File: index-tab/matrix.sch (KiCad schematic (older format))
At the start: 0 parts

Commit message: Added MX alps hybrid symbol to the library
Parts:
- added MX? (x76): MX-LED, symbol MX_Alps_Hybrid:MX-LED

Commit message: Trying to make the library path indepented
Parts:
- MX? (x76): symbol MX_Alps_Hybrid:MX-LED -> index-tab-rescue:MX-LED-MX_Alps_Hybrid

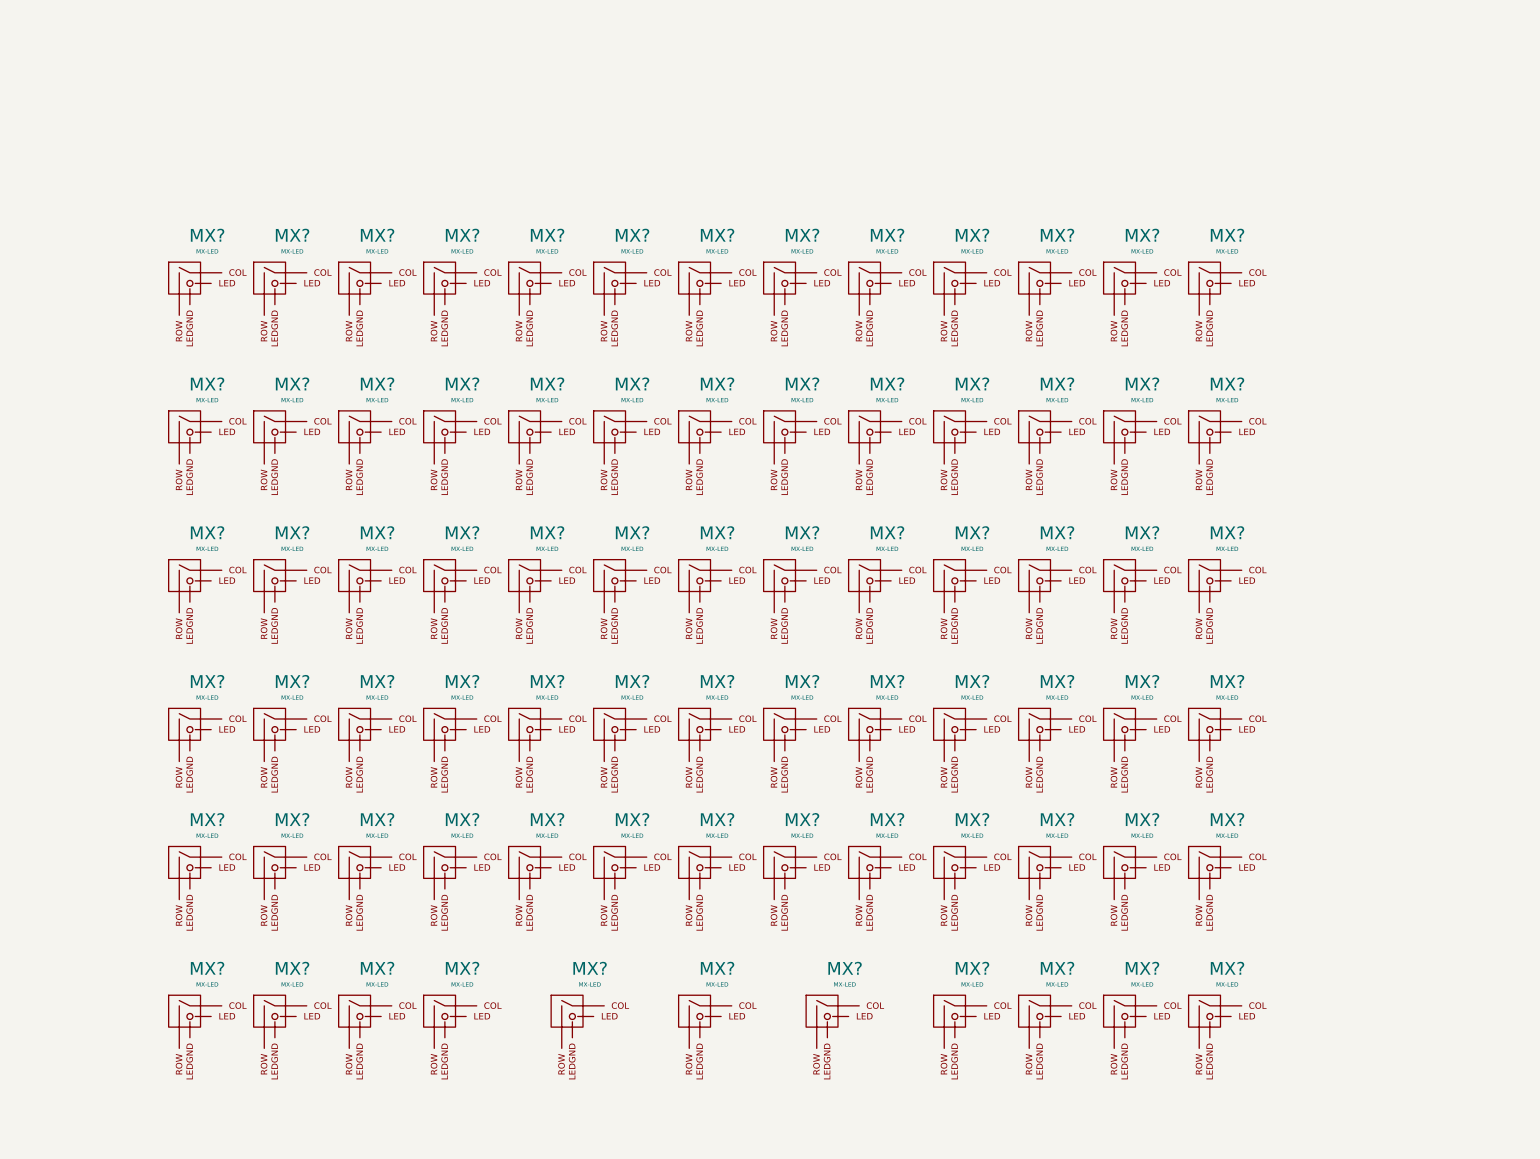
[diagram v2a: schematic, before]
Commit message: Change to u4, added files for backlight and rgb
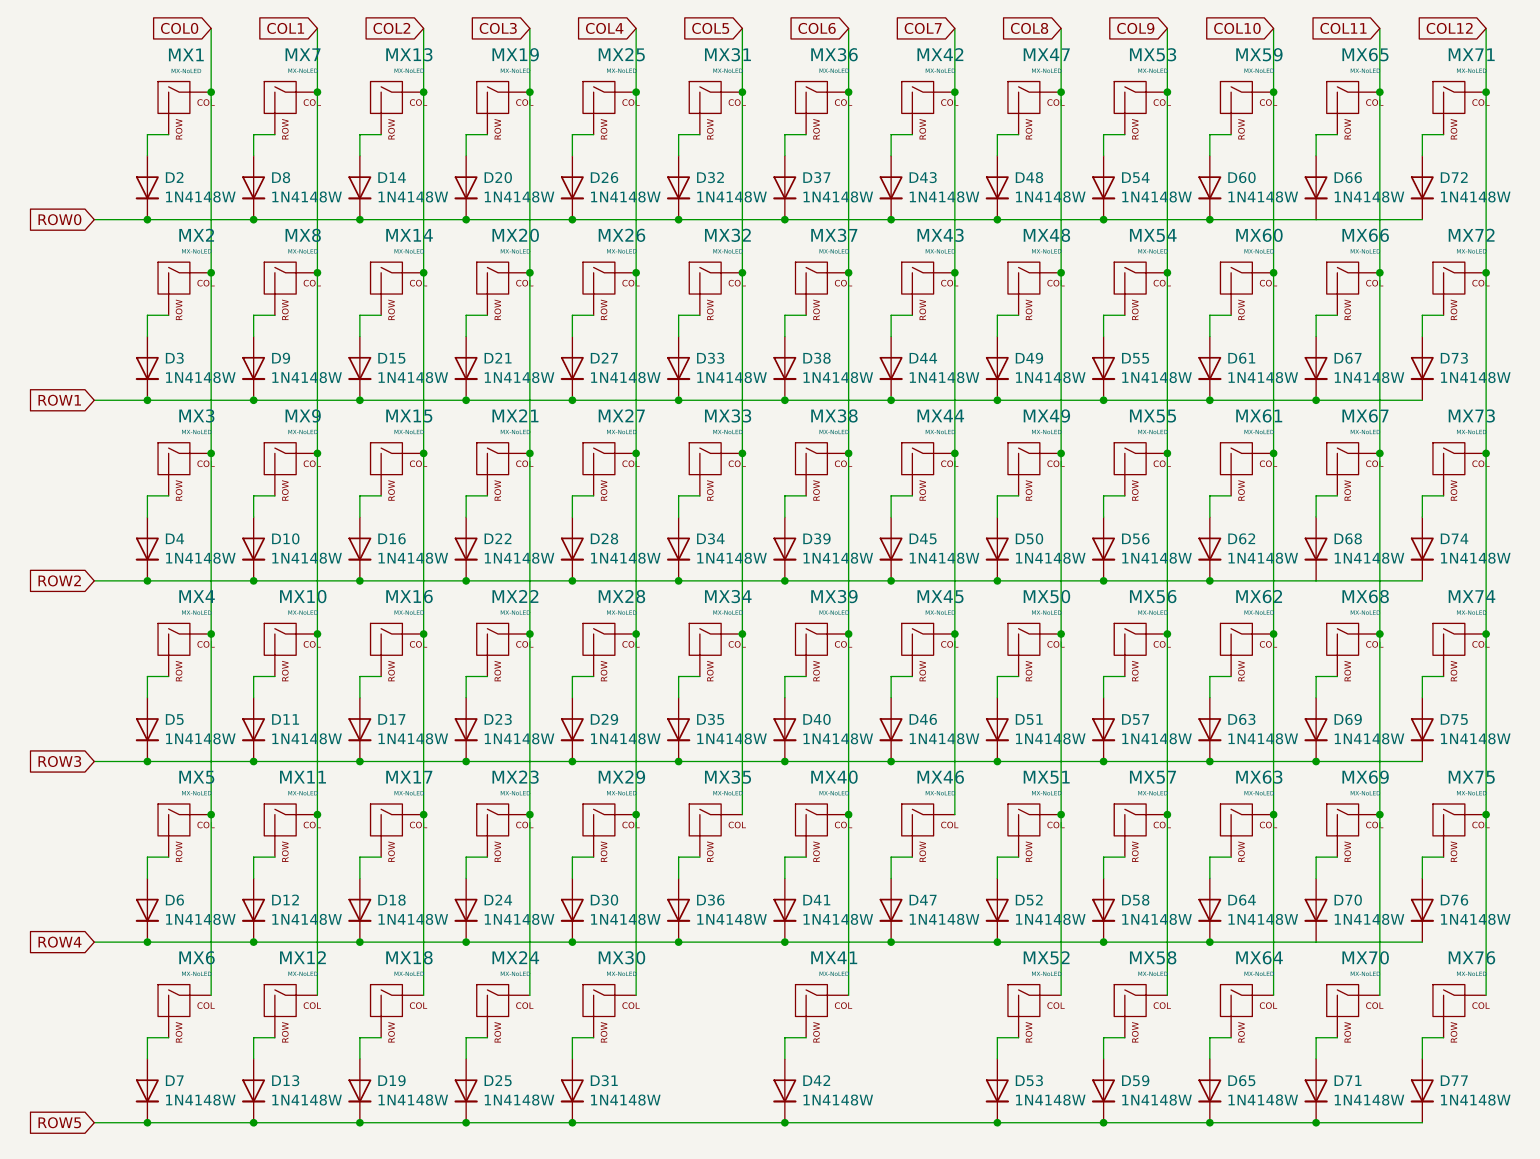
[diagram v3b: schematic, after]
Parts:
- removed MX? (x76): MX-LED, symbol index-tab-rescue:MX-LED-MX_Alps_Hybrid
- added D10, D11, D12, D13, D14, D15, D16, D17, D18, D19, D2, D20, D21, D22, D23, D24, D25, D26, D27, D28, D29, D3, D30, D31, D32, D33, D34, D35, D36, D37, D38, D39, D4, D40, D41, D42, D43, D44, D45, D46, D47, D48, D49, D5, D50, D51, D52, D53, D54, D55, D56, D57, D58, D59, D6, D60, D61, D62, D63, D64, D65, D66, D67, D68, D69, D7, D70, D71, D72, D73, D74, D75, D76, D77, D8, D9: 1N4148W, Diode_SMD:D_SOD-123, symbol Diode:1N4148W
- added MX1, MX10, MX11, MX12, MX13, MX14, MX15, MX16, MX17, MX18, MX19, MX2, MX20, MX21, MX22, MX23, MX24, MX25, MX26, MX27, MX28, MX29, MX3, MX30, MX31, MX32, MX33, MX34, MX35, MX36, MX37, MX38, MX39, MX4, MX40, MX41, MX42, MX43, MX44, MX45, MX46, MX47, MX48, MX49, MX5, MX50, MX51, MX52, MX53, MX54, MX55, MX56, MX57, MX58, MX59, MX6, MX60, MX61, MX62, MX63, MX64, MX65, MX66, MX67, MX68, MX69, MX7, MX70, MX71, MX72, MX73, MX74, MX75, MX76, MX8, MX9: MX-NoLED, symbol MX_Alps_Hybrid:MX-NoLED
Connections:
- new net: D2.2 (A), MX1.2 (ROW)
- new net: D8.2 (A), MX7.2 (ROW)
- new net: D14.2 (A), MX13.2 (ROW)
- new net: D20.2 (A), MX19.2 (ROW)
- new net: D26.2 (A), MX25.2 (ROW)
- new net: D32.2 (A), MX31.2 (ROW)
- new net: D37.2 (A), MX36.2 (ROW)
- new net: D43.2 (A), MX42.2 (ROW)
- new net: D48.2 (A), MX47.2 (ROW)
- new net: D54.2 (A), MX53.2 (ROW)
- new net: D60.2 (A), MX59.2 (ROW)
- new net: D66.2 (A), MX65.2 (ROW)
- new net: D72.2 (A), MX71.2 (ROW)
- new net: D3.2 (A), MX2.2 (ROW)
- new net: D9.2 (A), MX8.2 (ROW)
- new net: D15.2 (A), MX14.2 (ROW)
- new net: D21.2 (A), MX20.2 (ROW)
- new net: D27.2 (A), MX26.2 (ROW)
- new net: D33.2 (A), MX32.2 (ROW)
- new net: D38.2 (A), MX37.2 (ROW)
- new net: D44.2 (A), MX43.2 (ROW)
- new net: D49.2 (A), MX48.2 (ROW)
- new net: D55.2 (A), MX54.2 (ROW)
- new net: D61.2 (A), MX60.2 (ROW)
- new net: D67.2 (A), MX66.2 (ROW)
- new net: D73.2 (A), MX72.2 (ROW)
- new net: D4.2 (A), MX3.2 (ROW)
- new net: D10.2 (A), MX9.2 (ROW)
- new net: D16.2 (A), MX15.2 (ROW)
- new net: D22.2 (A), MX21.2 (ROW)
- new net: D28.2 (A), MX27.2 (ROW)
- new net: D34.2 (A), MX33.2 (ROW)
- new net: D39.2 (A), MX38.2 (ROW)
- new net: D45.2 (A), MX44.2 (ROW)
- new net: D50.2 (A), MX49.2 (ROW)
- new net: D56.2 (A), MX55.2 (ROW)
- new net: D62.2 (A), MX61.2 (ROW)
- new net: D68.2 (A), MX67.2 (ROW)
- new net: D74.2 (A), MX73.2 (ROW)
- new net: D5.2 (A), MX4.2 (ROW)
- new net: D11.2 (A), MX10.2 (ROW)
- new net: D17.2 (A), MX16.2 (ROW)
- new net: D23.2 (A), MX22.2 (ROW)
- new net: D29.2 (A), MX28.2 (ROW)
- new net: D35.2 (A), MX34.2 (ROW)
- new net: D40.2 (A), MX39.2 (ROW)
- new net: D46.2 (A), MX45.2 (ROW)
- new net: D51.2 (A), MX50.2 (ROW)
- new net: D57.2 (A), MX56.2 (ROW)
- new net: D63.2 (A), MX62.2 (ROW)
- new net: D69.2 (A), MX68.2 (ROW)
- new net: D75.2 (A), MX74.2 (ROW)
- new net: D6.2 (A), MX5.2 (ROW)
- new net: D12.2 (A), MX11.2 (ROW)
- new net: D18.2 (A), MX17.2 (ROW)
- new net: D24.2 (A), MX23.2 (ROW)
- new net: D30.2 (A), MX29.2 (ROW)
- new net: D36.2 (A), MX35.2 (ROW)
- new net: D41.2 (A), MX40.2 (ROW)
- new net: D47.2 (A), MX46.2 (ROW)
- new net: D52.2 (A), MX51.2 (ROW)
- new net: D58.2 (A), MX57.2 (ROW)
- new net: D64.2 (A), MX63.2 (ROW)
- new net: D70.2 (A), MX69.2 (ROW)
- new net: D76.2 (A), MX75.2 (ROW)
- new net: D7.2 (A), MX6.2 (ROW)
- new net: D13.2 (A), MX12.2 (ROW)
- new net: D19.2 (A), MX18.2 (ROW)
- new net: D25.2 (A), MX24.2 (ROW)
- new net: D31.2 (A), MX30.2 (ROW)
- new net: D42.2 (A), MX41.2 (ROW)
- new net: D53.2 (A), MX52.2 (ROW)
- new net: D59.2 (A), MX58.2 (ROW)
- new net: D65.2 (A), MX64.2 (ROW)
- new net: D71.2 (A), MX70.2 (ROW)
- new net: D77.2 (A), MX76.2 (ROW)
- new net COL0: MX1.1 (COL), MX2.1 (COL), MX3.1 (COL), MX4.1 (COL), MX5.1 (COL), MX6.1 (COL)
- new net COL1: MX10.1 (COL), MX11.1 (COL), MX12.1 (COL), MX7.1 (COL), MX8.1 (COL), MX9.1 (COL)
- new net COL10: MX59.1 (COL), MX60.1 (COL), MX61.1 (COL), MX62.1 (COL), MX63.1 (COL), MX64.1 (COL)
- new net COL11: MX65.1 (COL), MX66.1 (COL), MX67.1 (COL), MX68.1 (COL), MX69.1 (COL), MX70.1 (COL)
- new net COL12: MX71.1 (COL), MX72.1 (COL), MX73.1 (COL), MX74.1 (COL), MX75.1 (COL), MX76.1 (COL)
- new net COL2: MX13.1 (COL), MX14.1 (COL), MX15.1 (COL), MX16.1 (COL), MX17.1 (COL), MX18.1 (COL)
- new net COL3: MX19.1 (COL), MX20.1 (COL), MX21.1 (COL), MX22.1 (COL), MX23.1 (COL), MX24.1 (COL)
- new net COL4: MX25.1 (COL), MX26.1 (COL), MX27.1 (COL), MX28.1 (COL), MX29.1 (COL), MX30.1 (COL)
- new net COL5: MX31.1 (COL), MX32.1 (COL), MX33.1 (COL), MX34.1 (COL), MX35.1 (COL)
- new net COL6: MX36.1 (COL), MX37.1 (COL), MX38.1 (COL), MX39.1 (COL), MX40.1 (COL), MX41.1 (COL)
- new net COL7: MX42.1 (COL), MX43.1 (COL), MX44.1 (COL), MX45.1 (COL), MX46.1 (COL)
- new net COL8: MX47.1 (COL), MX48.1 (COL), MX49.1 (COL), MX50.1 (COL), MX51.1 (COL), MX52.1 (COL)
- new net COL9: MX53.1 (COL), MX54.1 (COL), MX55.1 (COL), MX56.1 (COL), MX57.1 (COL), MX58.1 (COL)
- new net ROW0: D14.1 (K), D2.1 (K), D20.1 (K), D26.1 (K), D32.1 (K), D37.1 (K), D43.1 (K), D48.1 (K), D54.1 (K), D60.1 (K), D66.1 (K), D72.1 (K), D8.1 (K)
- new net ROW1: D15.1 (K), D21.1 (K), D27.1 (K), D3.1 (K), D33.1 (K), D38.1 (K), D44.1 (K), D49.1 (K), D55.1 (K), D61.1 (K), D67.1 (K), D73.1 (K), D9.1 (K)
- new net ROW2: D10.1 (K), D16.1 (K), D22.1 (K), D28.1 (K), D34.1 (K), D39.1 (K), D4.1 (K), D45.1 (K), D50.1 (K), D56.1 (K), D62.1 (K), D68.1 (K), D74.1 (K)
- new net ROW3: D11.1 (K), D17.1 (K), D23.1 (K), D29.1 (K), D35.1 (K), D40.1 (K), D46.1 (K), D5.1 (K), D51.1 (K), D57.1 (K), D63.1 (K), D69.1 (K), D75.1 (K)
- new net ROW4: D12.1 (K), D18.1 (K), D24.1 (K), D30.1 (K), D36.1 (K), D41.1 (K), D47.1 (K), D52.1 (K), D58.1 (K), D6.1 (K), D64.1 (K), D70.1 (K), D76.1 (K)
- new net ROW5: D13.1 (K), D19.1 (K), D25.1 (K), D31.1 (K), D42.1 (K), D53.1 (K), D59.1 (K), D65.1 (K), D7.1 (K), D71.1 (K), D77.1 (K)

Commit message: Added footprints to all components, and done some formatting
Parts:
- MX1, MX10, MX11, MX12, MX13, MX14, MX15, MX16, MX17, MX18, MX19, MX2, MX20, MX21, MX22, MX23, MX24, MX25, MX26, MX27, MX28, MX29, MX3, MX31, MX32, MX33, MX34, MX35, MX36, MX37, MX38, MX39, MX4, MX40, MX41, MX42, MX43, MX44, MX45, MX46, MX47, MX48, MX49, MX5, MX50, MX51, MX53, MX54, MX55, MX56, MX57, MX58, MX59, MX6, MX60, MX61, MX62, MX63, MX64, MX65, MX66, MX67, MX68, MX69, MX7, MX70, MX71, MX72, MX73, MX74, MX75, MX76, MX8, MX9: footprint (none) -> index-tab:Kailh_socket_MX
- MX30, MX52: footprint (none) -> index-tab:Stabilizer_MX_2u
